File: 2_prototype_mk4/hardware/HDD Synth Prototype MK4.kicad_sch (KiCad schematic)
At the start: 1 part

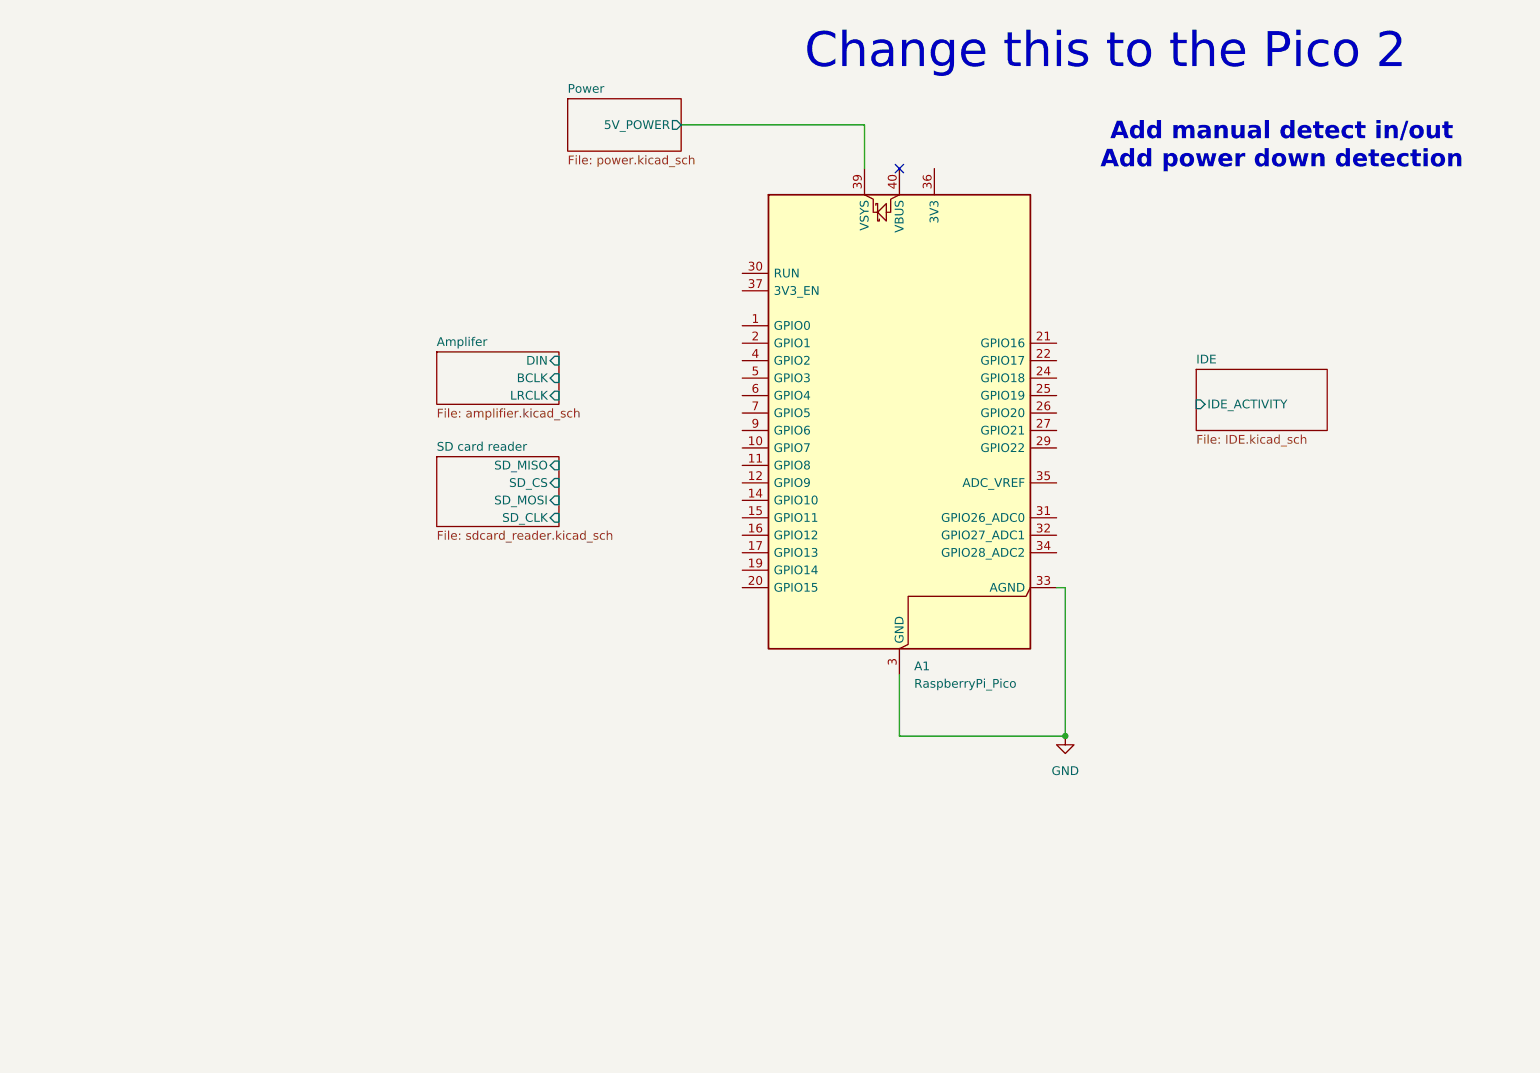
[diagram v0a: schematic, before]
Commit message: Create initial MK4 PCB layout
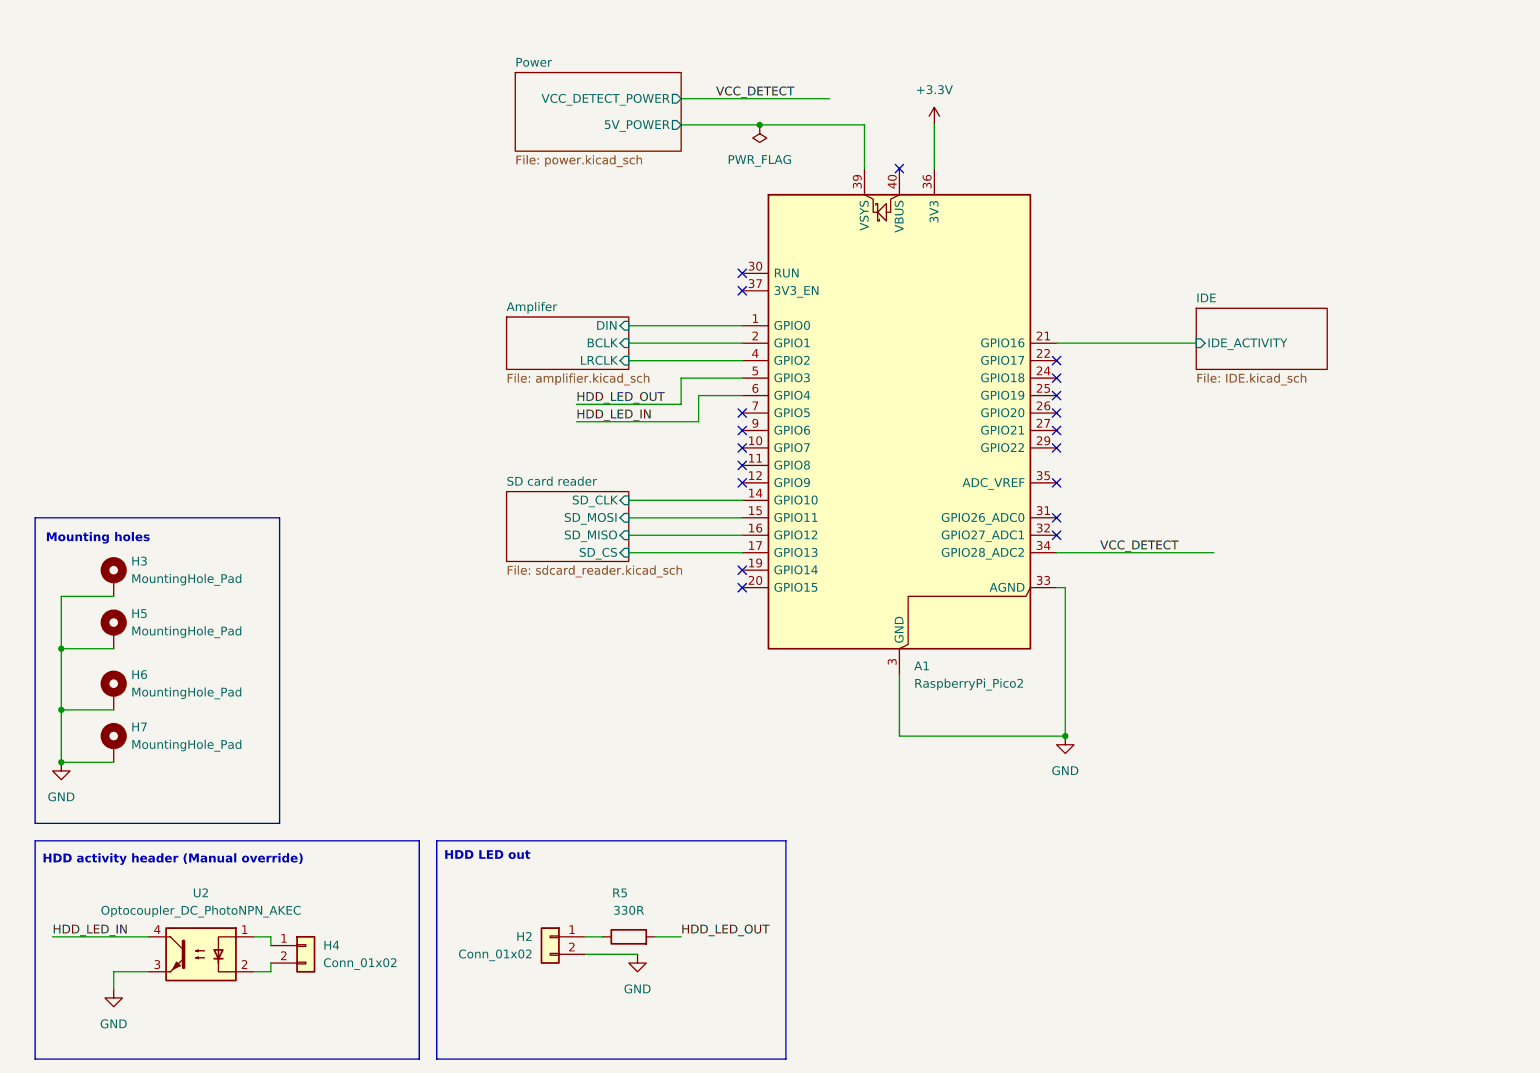
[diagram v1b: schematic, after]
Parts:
- added H2, H4: Conn_01x02, Connector_PinHeader_2.54mm:PinHeader_1x02_P2.54mm_Vertical, symbol Connector_Generic:Conn_01x02
- added H3, H5, H6, H7: MountingHole_Pad, MountingHole:MountingHole_3.2mm_M3_Pad, symbol Mechanical:MountingHole_Pad
- added R5: 330R, Resistor_SMD:R_0603_1608Metric, symbol Device:R
- added U2: Optocoupler_DC_PhotoNPN_AKEC, Package_SO:SO-4_4.4x3.6mm_P2.54mm, symbol Isolator:Optocoupler_DC_PhotoNPN_AKEC
- A1: value RaspberryPi_Pico -> RaspberryPi_Pico2
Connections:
- net Amplifer/BCLK: now also A1.2 (GPIO1)
- net Amplifer/DIN: now also A1.1 (GPIO0)
- net Amplifer/LRCLK: now also A1.4 (GPIO2)
- net GND: now also H2.2 (Pin_2), H3.1, H5.1, H6.1, H7.1, U2.3
- net IDE/IDE_ACTIVITY: now also A1.21 (GPIO16)
- net SD card reader/SD_CLK: now also A1.14 (GPIO10)
- net SD card reader/SD_CS: now also A1.17 (GPIO13)
- net SD card reader/SD_MISO: now also A1.16 (GPIO12)
- net SD card reader/SD_MOSI: now also A1.15 (GPIO11)
- net VCC_DETECT: now reaches A1.34 (GPIO28_ADC2)
- net +3.3V: now reaches A1.36 (3V3)
- net HDD_LED_OUT: now reaches A1.5 (GPIO3)
- net HDD_LED_OUT: now also R5.2
- net HDD_LED_IN: now reaches A1.6 (GPIO4)
- net HDD_LED_IN: now also U2.4
- new net: H2.1 (Pin_1), R5.1
- new net: H4.1 (Pin_1), U2.1
- new net: H4.2 (Pin_2), U2.2
- no-connect marks 1 -> 19
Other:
- sheet Power ports: added VCC_DETECT_POWER; removed none
- note added: "HDD LED out"
- note added: "HDD activity header (Manual override)"
- note added: "Mounting holes"
- note removed: "Add manual detect in/out Add power down detection"
- note removed: "Change this to the Pico 2"

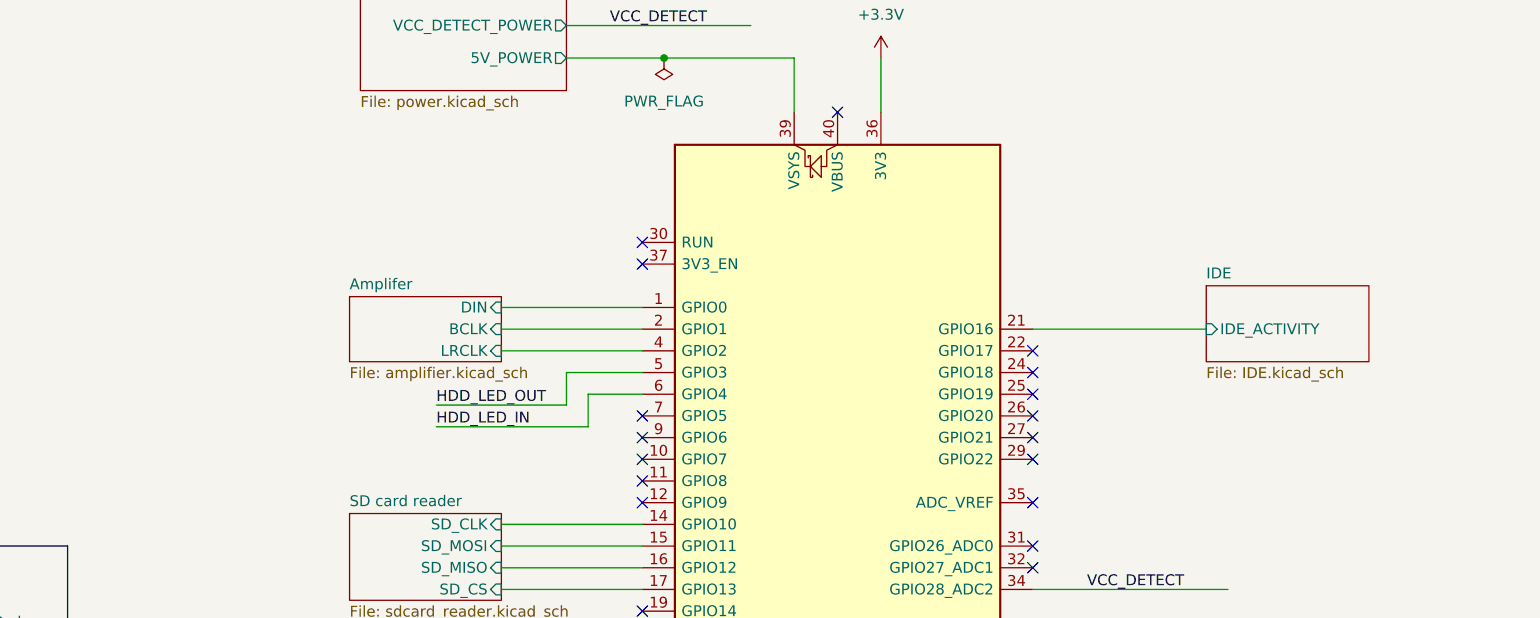
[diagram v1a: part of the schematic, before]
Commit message: Placed all components on PCB
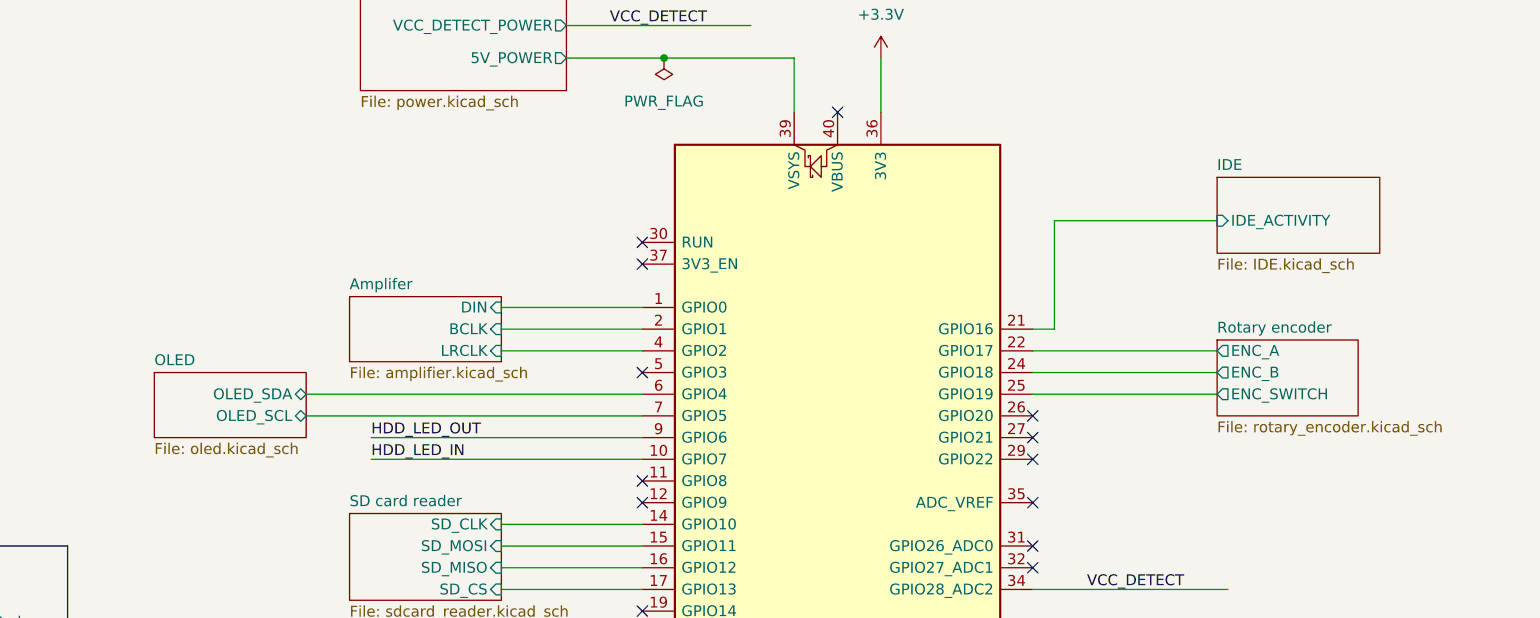
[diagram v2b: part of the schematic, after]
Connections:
- net HDD_LED_IN: now also A1.10 (GPIO7); no longer A1.6 (GPIO4)
- net HDD_LED_OUT: now also A1.9 (GPIO6); no longer A1.5 (GPIO3)
- net Rotary encoder/ENC_A: now reaches A1.22 (GPIO17)
- net Rotary encoder/ENC_B: now reaches A1.24 (GPIO18)
- net Rotary encoder/ENC_SWITCH: now reaches A1.25 (GPIO19)
- net OLED/OLED_SCL: now reaches A1.7 (GPIO5)
- new net OLED/OLED_SDA: A1.6 (GPIO4)
- no-connect marks 19 -> 14
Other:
- added sheet OLED (oled.kicad_sch)
- added sheet Rotary encoder (rotary_encoder.kicad_sch)
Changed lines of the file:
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@@
-	)
-	(no_connect
-		(at 167.64 92.71)
-	)
-	(no_connect
-		(at 167.64 87.63)
 	)
 	(no_connect
@@
 	)
 	(no_connect
-		(at 121.92 97.79)
-	)
-	(no_connect
-		(at 121.92 95.25)
+		(at 121.92 90.17)
 	)
 	(no_connect
@@
 	)
 	(no_connect
-		(at 121.92 100.33)
-	)
-	(no_connect
 		(at 121.92 120.65)
 	)
@@
 	)
 	(no_connect
-		(at 167.64 90.17)
-	)
-	(no_connect
 		(at 121.92 118.11)
 	)
 	(wire
 		(pts
-			(xy 97.79 96.52) (xy 115.57 96.52)
-		)
-		(stroke
-			(width 0)
-			(type default)
-		)
-	)
-	(wire
-		(pts
-			(xy 115.57 92.71) (xy 115.57 96.52)
+			(xy 90.17 100.33) (xy 121.92 100.33)
+		)
+		(stroke
+			(width 0)
+			(type default)
+		)
+	)
+	(wire
+		(pts
+			(xy 167.64 90.17) (xy 189.23 90.17)
 		)
 		(stroke
@@
 	(wire
 		(pts
-			(xy 121.92 92.71) (xy 115.57 92.71)
-		)
-		(stroke
-			(width 0)
-			(type default)
-		)
-	)
-	(wire
-		(pts
 			(xy 30.48 176.53) (xy 30.48 179.07)
 		)
@@
 	(wire
 		(pts
-			(xy 113.03 90.17) (xy 113.03 93.98)
-		)
-		(stroke
-			(width 0)
-			(type default)
-		)
-	)
-	(wire
-		(pts
 			(xy 113.03 49.53) (xy 134.62 49.53)
 		)
@@
 	(wire
 		(pts
-			(xy 167.64 85.09) (xy 187.96 85.09)
+			(xy 170.18 72.39) (xy 170.18 85.09)
+		)
+		(stroke
+			(width 0)
+			(type default)
+		)
+	)
+	(wire
+		(pts
+			(xy 170.18 72.39) (xy 189.23 72.39)
 		)
 		(stroke
@@
 	(wire
 		(pts
-			(xy 97.79 93.98) (xy 113.03 93.98)
+			(xy 90.17 97.79) (xy 121.92 97.79)
 		)
 		(stroke
@@
 	(wire
 		(pts
+			(xy 167.64 85.09) (xy 170.18 85.09)
+		)
+		(stroke
+			(width 0)
+			(type default)
+		)
+	)
+	(wire
+		(pts
 			(xy 109.22 171.45) (xy 113.03 171.45)
 		)
@@
 	(wire
 		(pts
+			(xy 167.64 92.71) (xy 189.23 92.71)
+		)
+		(stroke
+			(width 0)
+			(type default)
+		)
+	)
+	(wire
+		(pts
 			(xy 124.46 53.34) (xy 139.7 53.34)
 		)
@@
 	(wire
 		(pts
+			(xy 82.55 95.25) (xy 121.92 95.25)
+		)
+		(stroke
+			(width 0)
+			(type default)
+		)
+	)
+	(wire
+		(pts
+			(xy 82.55 92.71) (xy 121.92 92.71)
+		)
+		(stroke
+			(width 0)
+			(type default)
+		)
+	)
+	(wire
+		(pts
 			(xy 53.34 171.45) (xy 53.34 172.72)
 		)
@@
 	(wire
 		(pts
-			(xy 121.92 90.17) (xy 113.03 90.17)
+			(xy 167.64 87.63) (xy 189.23 87.63)
 		)
 		(stroke
@@
 	)
 	(label "HDD_LED_IN"
-		(at 97.79 96.52 0)
+		(at 90.17 100.33 0)
 		(effects
 			(font
@@
 	)
 	(label "HDD_LED_OUT"
-		(at 97.79 93.98 0)
+		(at 90.17 97.79 0)
 		(effects
 			(font
@@
 	)
 	(sheet
-		(at 187.96 80.01)
+		(at 189.23 67.31)
 		(size 19.05 8.89)
 		(exclude_from_sim no)
@@
 		)
 		(property "Sheetname" "IDE"
-			(at 187.96 79.2984 0)
+			(at 189.23 66.5984 0)
 			(show_name no)
 			(do_not_autoplace no)
@@
 		)
 		(property "Sheetfile" "IDE.kicad_sch"
-			(at 187.96 89.4846 0)
+			(at 189.23 76.7846 0)
 			(show_name no)
 			(do_not_autoplace no)
@@
 		)
 		(pin "IDE_ACTIVITY" input
-			(at 187.96 85.09 180)
+			(at 189.23 72.39 180)
 			(effects
 				(font
@@
 				(path "/1a22431a-ba36-40a0-9a7e-c2a82ec69c53"
 					(page "5")
+				)
+			)
+		)
+	)
+	(sheet
+		(at 189.23 86.36)
+		(size 16.51 8.89)
+		(exclude_from_sim no)
+		(in_bom yes)
+		(on_board yes)
+		(dnp no)
+		(fields_autoplaced yes)
+		(stroke
+			(width 0.1524)
+			(type solid)
+		)
+		(fill
+			(color 0 0 0 0)
+		)
+		(property "Sheetname" "Rotary encoder"
+			(at 189.23 85.6484 0)
+			(show_name no)
+			(do_not_autoplace no)
+			(effects
+				(font
+					(size 1.27 1.27)
+				)
+				(justify left bottom)
+			)
+		)
+		(property "Sheetfile" "rotary_encoder.kicad_sch"
+			(at 189.23 95.8346 0)
+			(show_name no)
+			(do_not_autoplace no)
+			(effects
+				(font
+					(size 1.27 1.27)
+				)
+				(justify left top)
+			)
+		)
+		(pin "ENC_SWITCH" output
+			(at 189.23 92.71 180)
+			(effects
+				(font
+					(size 1.27 1.27)
+				)
+				(justify left)
+			)
+		)
+		(pin "ENC_B" output
+			(at 189.23 90.17 180)
+			(effects
+				(font
+					(size 1.27 1.27)
+				)
+				(justify left)
+			)
+		)
+		(pin "ENC_A" output
+			(at 189.23 87.63 180)
+			(effects
+				(font
+					(size 1.27 1.27)
+				)
+				(justify left)
+			)
+		)
+		(instances
+			(project "HDD Synth Prototype MK4"
+				(path "/1a22431a-ba36-40a0-9a7e-c2a82ec69c53"
+					(page "7")
 				)
 			)
@@
 				)
 			)
+		)
+	)
+	(sheet
+		(at 64.77 90.17)
+		(size 17.78 7.62)
+		(exclude_from_sim no)
+		(in_bom yes)
+		(on_board yes)
+		(dnp no)
+		(fields_autoplaced yes)
+		(stroke
+			(width 0.1524)
+			(type solid)
+		)
+		(fill
+			(color 0 0 0 0)
+		)
+		(property "Sheetname" "OLED"
+			(at 64.77 89.4584 0)
+			(show_name no)
+			(do_not_autoplace no)
+			(effects
+				(font
+					(size 1.27 1.27)
+				)
+				(justify left bottom)
+			)
+		)
+		(property "Sheetfile" "oled.kicad_sch"
+			(at 64.77 98.3746 0)
+			(show_name no)
+			(do_not_autoplace no)
+			(effects
+				(font
+					(size 1.27 1.27)
+				)
+				(justify left top)
+			)
+		)
+		(pin "OLED_SCL" bidirectional
+			(at 82.55 95.25 0)
+			(effects
+				(font
+					(size 1.27 1.27)
+				)
+				(justify right)
+			)
+		)
+		(pin "OLED_SDA" bidirectional
+			(at 82.55 92.71 0)
+			(effects
+				(font
+					(size 1.27 1.27)
+				)
+				(justify right)
+			)
+		)
+		(instances
+			(project "HDD Synth Prototype MK4"
+				(path "/1a22431a-ba36-40a0-9a7e-c2a82ec69c53"
+					(page "6")
+				)
+			)

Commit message: Update MKIV hardware & use MKIII software as basic for MKIV
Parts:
- U2: Manufacturer Everlight -> (none)
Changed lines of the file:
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@@
-			)
-		)
-		(property "Manufacturer" ""
-			(at 93.98 171.45 0)
-			(hide yes)
-			(show_name no)
-			(do_not_autoplace no)
-			(effects
-				(font
-					(size 1.27 1.27)
-				)
 			)
 		)
@@
 			)
 		)
-		(property "Manufacturer" ""
-			(at 58.42 172.72 0)
-			(hide yes)
-			(show_name no)
-			(do_not_autoplace no)
-			(effects
-				(font
-					(size 1.27 1.27)
-				)
-			)
-		)
 		(property "LCSC_Part_Number" ""
 			(at 58.42 172.72 0)
@@
 			)
 		)
-		(property "Manufacturer" "Everlight"
-			(at 43.18 173.99 0)
-			(hide yes)
-			(show_name no)
-			(do_not_autoplace no)
-			(effects
-				(font
-					(size 1.27 1.27)
-				)
-			)
-		)
 		(property "LCSC_Part_Number" "C2916312"
 			(at 43.18 173.99 0)
@@
 			(at 105.41 171.45 90)
 			(hide yes)
-			(show_name no)
-			(do_not_autoplace no)
-			(effects
-				(font
-					(size 1.27 1.27)
-				)
-			)
-		)
-		(property "Manufacturer" ""
-			(at 105.41 171.45 90)
-			(hide yes)

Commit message: Final MKIV tweaks before sending off to PCBWay
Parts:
- added H8: Conn_01x02, Connector_PinHeader_2.54mm:PinHeader_1x02_P2.54mm_Vertical, symbol Connector_Generic:Conn_01x02
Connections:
- net GND: now also H8.2 (Pin_2)
- net ACTION_BTN: now reaches A1.26 (GPIO20)
- net ACTION_BTN: now also H8.1 (Pin_1)
- net Reset/PICO_RUN: now reaches A1.30 (RUN)
- net Amplifer/SD_MODE: now reaches A1.5 (GPIO3)
- no-connect marks 14 -> 11
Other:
- added sheet Reset (reset.kicad_sch)
- sheet Amplifer ports: added SD_MODE; removed none
- sheet IDE ports: added IDE_RESET; removed none
- note added: "Action button"

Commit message: MKIV add RGB LED, reset jumper and fixed reset circuit
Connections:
- net RGB LED/RGB_DATA: now reaches A1.19 (GPIO14)
- no-connect marks 11 -> 10
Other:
- added sheet RGB LED (rgb_led.kicad_sch)
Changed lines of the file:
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@@
 		(at 167.64 97.79)
 	)
-	(no_connect
-		(at 121.92 118.11)
-	)
 	(wire
 		(pts
@@
 	(wire
 		(pts
+			(xy 105.41 128.27) (xy 118.11 128.27)
+		)
+		(stroke
+			(width 0)
+			(type default)
+		)
+	)
+	(wire
+		(pts
 			(xy 167.64 95.25) (xy 184.15 95.25)
 		)
@@
 	(wire
 		(pts
+			(xy 121.92 118.11) (xy 118.11 118.11)
+		)
+		(stroke
+			(width 0)
+			(type default)
+		)
+	)
+	(wire
+		(pts
 			(xy 53.34 171.45) (xy 53.34 172.72)
 		)
@@
 		(pts
 			(xy 105.41 115.57) (xy 121.92 115.57)
+		)
+		(stroke
+			(width 0)
+			(type default)
+		)
+	)
+	(wire
+		(pts
+			(xy 118.11 118.11) (xy 118.11 128.27)
 		)
 		(stroke
@@
 				)
 			)
+		)
+	)
+	(sheet
+		(at 87.63 125.73)
+		(size 17.78 5.08)
+		(exclude_from_sim no)
+		(in_bom yes)
+		(on_board yes)
+		(dnp no)
+		(fields_autoplaced yes)
+		(stroke
+			(width 0.1524)
+			(type solid)
+		)
+		(fill
+			(color 0 0 0 0)
+		)
+		(property "Sheetname" "RGB LED"
+			(at 87.63 125.0184 0)
+			(show_name no)
+			(do_not_autoplace no)
+			(effects
+				(font
+					(size 1.27 1.27)
+				)
+				(justify left bottom)
+			)
+		)
+		(property "Sheetfile" "rgb_led.kicad_sch"
+			(at 87.63 131.3946 0)
+			(show_name no)
+			(do_not_autoplace no)
+			(effects
+				(font
+					(size 1.27 1.27)
+				)
+				(justify left top)
+			)
+		)
+		(pin "RGB_DATA" input
+			(at 105.41 128.27 0)
+			(effects
+				(font
+					(size 1.27 1.27)
+				)
+				(justify right)
+			)
+		)
+		(instances
+			(project "HDD Synth Prototype MK4"
+				(path "/1a22431a-ba36-40a0-9a7e-c2a82ec69c53"
+					(page "9")
+				)
+			)
